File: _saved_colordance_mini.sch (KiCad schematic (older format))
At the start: 69 parts, among them J1 XLR3, J10 CONN_01X06, J11 CONN_01X04, J12 CONN_01X04, J13 CONN_01X03, J14 CONN_01X03, J15 CONN_01X03, J16 CONN_01X03, J17 CONN_01X04, J2 CONN_01X08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

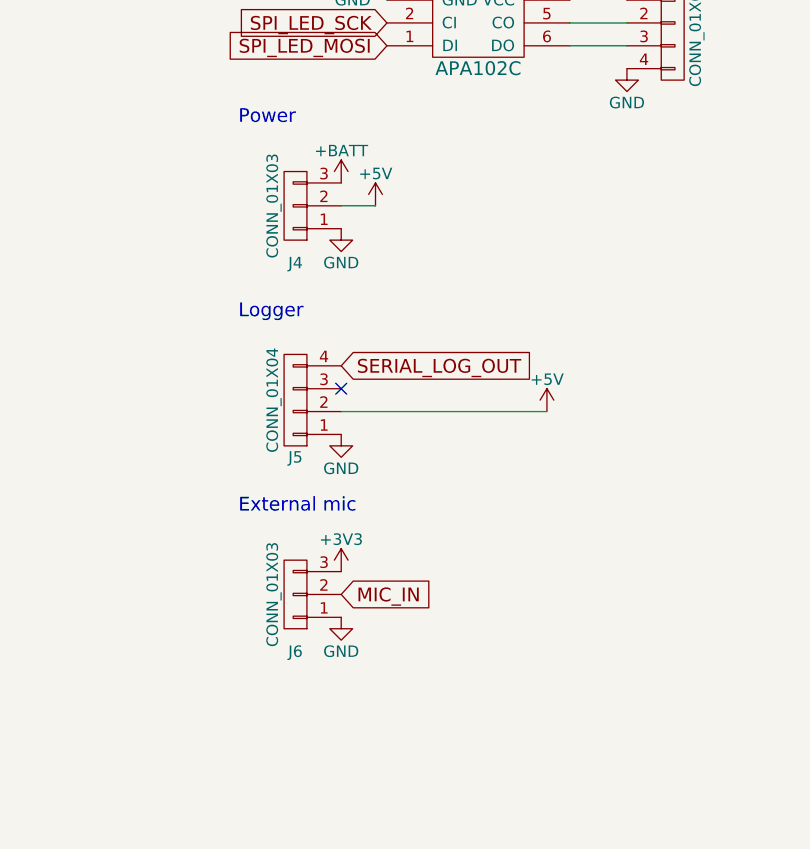
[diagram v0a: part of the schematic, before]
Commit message: Rough placement
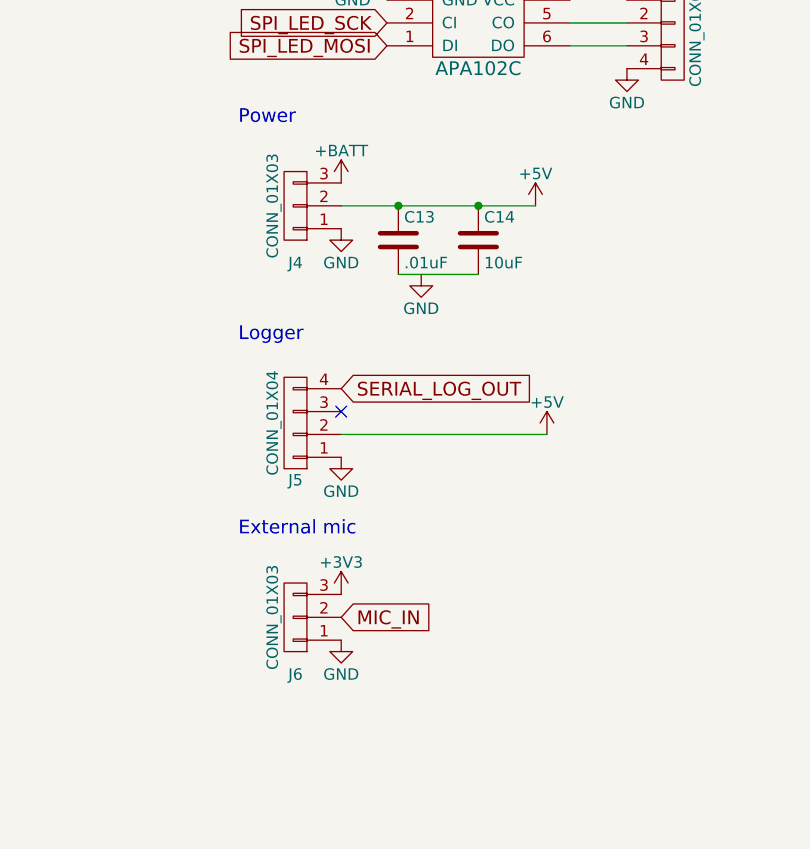
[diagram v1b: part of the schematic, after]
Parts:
- added C13: .01uF, Capacitors_SMD:C_0603_HandSoldering, symbol C
- added C14: 10uF, Capacitors_SMD:C_0603_HandSoldering, symbol C
- J1: footprint shardy:XLR-NC3FA -> homebrew:NC3FAH
- U1: footprint 21-0041B_8 -> SMD_Packages:SOIC-8-N
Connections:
- net +5V: now also C13.1, C14.1
- new net: C13.2, C14.2
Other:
- moved on the sheet: J5, J6
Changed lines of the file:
@@
 F 0 "U1" H 3350 9300 60  0000 C CNN
 F 1 "MAX485CSA+" H 3350 9200 60  0000 C CNN
-F 2 "21-0041B_8" H 3350 9140 60  0001 C CNN
+F 2 "SMD_Packages:SOIC-8-N" H 3350 9140 60  0001 C CNN
 F 3 "" H 2550 8900 60  0000 C CNN
 	1    2550 8900
@@
 F 0 "J1" H 1400 9000 50  0000 C CNN
 F 1 "XLR3" H 1450 8500 50  0000 C CNN
-F 2 "shardy:XLR-NC3FA" H 1250 8750 50  0001 C CNN
+F 2 "homebrew:NC3FAH" H 1250 8750 50  0001 C CNN
 F 3 "" H 1250 8750 50  0001 C CNN
 	1    1250 8750
@@
 L +5V #PWR041
 U 1 1 5ABFF8A7
-P 12600 6400
-F 0 "#PWR041" H 12600 6250 50  0001 C CNN
-F 1 "+5V" H 12600 6540 50  0000 C CNN
-F 2 "" H 12600 6400 50  0001 C CNN
-F 3 "" H 12600 6400 50  0001 C CNN
-	1    12600 6400
+P 13300 6400
+F 0 "#PWR041" H 13300 6250 50  0001 C CNN
+F 1 "+5V" H 13300 6540 50  0000 C CNN
+F 2 "" H 13300 6400 50  0001 C CNN
+F 3 "" H 13300 6400 50  0001 C CNN
+	1    13300 6400
 	1    0    0    -1
 $EndComp
@@
 $EndComp
 Wire Wire Line
-	12600 6400 12450 6400
+	12450 6400 13300 6400
 $Comp
 L CONN_01X03 J13
@@
 L CONN_01X04 J5
 U 1 1 5AC053E1
-P 12250 7250
-F 0 "J5" H 12250 7500 50  0000 C CNN
-F 1 "CONN_01X04" V 12350 7250 50  0000 C CNN
-F 2 "Pin_Headers:Pin_Header_Straight_1x04_Pitch2.54mm" H 12250 7250 50  0001 C CNN
-F 3 "" H 12250 7250 50  0001 C CNN
-	1    12250 7250
-	-1   0    0    1
-$EndComp
-Text Notes 12000 6900 0    60   ~ 0
+P 12250 7350
+F 0 "J5" H 12250 7600 50  0000 C CNN
+F 1 "CONN_01X04" V 12350 7350 50  0000 C CNN
+F 2 "Pin_Headers:Pin_Header_Straight_1x04_Pitch2.54mm" H 12250 7350 50  0001 C CNN
+F 3 "" H 12250 7350 50  0001 C CNN
+	1    12250 7350
+	-1   0    0    1
+$EndComp
+Text Notes 12000 7000 0    60   ~ 0
 Logger
 $Comp
 L +5V #PWR052
 U 1 1 5AC053EA
-P 13350 7300
-F 0 "#PWR052" H 13350 7150 50  0001 C CNN
-F 1 "+5V" H 13350 7440 50  0000 C CNN
-F 2 "" H 13350 7300 50  0001 C CNN
-F 3 "" H 13350 7300 50  0001 C CNN
-	1    13350 7300
+P 13350 7400
+F 0 "#PWR052" H 13350 7250 50  0001 C CNN
+F 1 "+5V" H 13350 7540 50  0000 C CNN
+F 2 "" H 13350 7400 50  0001 C CNN
+F 3 "" H 13350 7400 50  0001 C CNN
+	1    13350 7400
 	1    0    0    -1
 $EndComp
@@
 L GND #PWR053
 U 1 1 5AC053F0
-P 12450 7400
-F 0 "#PWR053" H 12450 7150 50  0001 C CNN
-F 1 "GND" H 12450 7250 50  0000 C CNN
-F 2 "" H 12450 7400 50  0001 C CNN
-F 3 "" H 12450 7400 50  0001 C CNN
-	1    12450 7400
-	1    0    0    -1
-$EndComp
-NoConn ~ 12450 7200
-Text GLabel 12450 7100 2    60   Input ~ 0
+P 12450 7500
+F 0 "#PWR053" H 12450 7250 50  0001 C CNN
+F 1 "GND" H 12450 7350 50  0000 C CNN
+F 2 "" H 12450 7500 50  0001 C CNN
+F 3 "" H 12450 7500 50  0001 C CNN
+	1    12450 7500
+	1    0    0    -1
+$EndComp
+NoConn ~ 12450 7300
+Text GLabel 12450 7200 2    60   Input ~ 0
 SERIAL_LOG_OUT
 Wire Wire Line
-	13350 7300 12450 7300
+	13350 7400 12450 7400
 $Comp
 L CONN_01X03 J6
 U 1 1 5ABFBAB9
-P 12250 8100
-F 0 "J6" H 12250 8350 50  0000 C CNN
-F 1 "CONN_01X03" V 12350 8100 50  0000 C CNN
-F 2 "Pin_Headers:Pin_Header_Straight_1x03_Pitch2.54mm" H 12250 8100 50  0001 C CNN
-F 3 "" H 12250 8100 50  0001 C CNN
-	1    12250 8100
-	-1   0    0    1
-$EndComp
-Text Notes 12000 7750 0    60   ~ 0
+P 12250 8200
+F 0 "J6" H 12250 8450 50  0000 C CNN
+F 1 "CONN_01X03" V 12350 8200 50  0000 C CNN
+F 2 "Pin_Headers:Pin_Header_Straight_1x03_Pitch2.54mm" H 12250 8200 50  0001 C CNN
+F 3 "" H 12250 8200 50  0001 C CNN
+	1    12250 8200
+	-1   0    0    1
+$EndComp
+Text Notes 12000 7850 0    60   ~ 0
 External mic
 $Comp
 L GND #PWR054
 U 1 1 5ABFBAC6
-P 12450 8200
-F 0 "#PWR054" H 12450 7950 50  0001 C CNN
-F 1 "GND" H 12450 8050 50  0000 C CNN
-F 2 "" H 12450 8200 50  0001 C CNN
-F 3 "" H 12450 8200 50  0001 C CNN
-	1    12450 8200
+P 12450 8300
+F 0 "#PWR054" H 12450 8050 50  0001 C CNN
+F 1 "GND" H 12450 8150 50  0000 C CNN
+F 2 "" H 12450 8300 50  0001 C CNN
+F 3 "" H 12450 8300 50  0001 C CNN
+	1    12450 8300
 	1    0    0    -1
 $EndComp
@@
 L +3V3 #PWR055
 U 1 1 5ABFC360
-P 12450 8000
-F 0 "#PWR055" H 12450 7850 50  0001 C CNN
-F 1 "+3V3" H 12450 8140 50  0000 C CNN
-F 2 "" H 12450 8000 50  0001 C CNN
-F 3 "" H 12450 8000 50  0001 C CNN
-	1    12450 8000
-	1    0    0    -1
-$EndComp
-Text GLabel 12450 8100 2    60   Input ~ 0
+P 12450 8100
+F 0 "#PWR055" H 12450 7950 50  0001 C CNN
+F 1 "+3V3" H 12450 8240 50  0000 C CNN
+F 2 "" H 12450 8100 50  0001 C CNN
+F 3 "" H 12450 8100 50  0001 C CNN
+	1    12450 8100
+	1    0    0    -1
+$EndComp
+Text GLabel 12450 8200 2    60   Input ~ 0
 MIC_IN
 Text GLabel 19050 4100 0    60   Input ~ 0
@@
 Wire Wire Line
 	13700 5700 13450 5700
+$Comp
+L C C13
+U 1 1 5AC21BC3
+P 12700 6550
+F 0 "C13" H 12725 6650 50  0000 L CNN
+F 1 ".01uF" H 12725 6450 50  0000 L CNN
+F 2 "Capacitors_SMD:C_0603_HandSoldering" H 12738 6400 50  0001 C CNN
+F 3 "" H 12700 6550 50  0001 C CNN
+	1    12700 6550
+	1    0    0    -1
+$EndComp
+$Comp
+L C C14
+U 1 1 5AC21CFD
+P 13050 6550
+F 0 "C14" H 13075 6650 50  0000 L CNN
+F 1 "10uF" H 13075 6450 50  0000 L CNN
+F 2 "Capacitors_SMD:C_0603_HandSoldering" H 13088 6400 50  0001 C CNN
+F 3 "" H 13050 6550 50  0001 C CNN
+	1    13050 6550
+	1    0    0    -1
+$EndComp
+Connection ~ 12700 6400
+Connection ~ 13050 6400
+Wire Wire Line
+	13050 6700 12700 6700
+$Comp
+L GND #PWR074
+U 1 1 5AC22B68
+P 12800 6700
+F 0 "#PWR074" H 12800 6450 50  0001 C CNN
+F 1 "GND" H 12800 6550 50  0000 C CNN
+F 2 "" H 12800 6700 50  0001 C CNN
+F 3 "" H 12800 6700 50  0001 C CNN
+	1    12800 6700
+	1    0    0    -1
+$EndComp
 $EndSCHEMATC
